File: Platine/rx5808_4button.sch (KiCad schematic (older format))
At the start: 61 parts, among them IC1 ATMEGA328-A, P1 CONN_01X02, P10 CONN_01X01, P11 CONN_01X01, P2 CONN_01X05, P3 CONN_02X03, P4 CONN_01X02, P5 BNC, P6 BNC, P7 CONN_01X02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

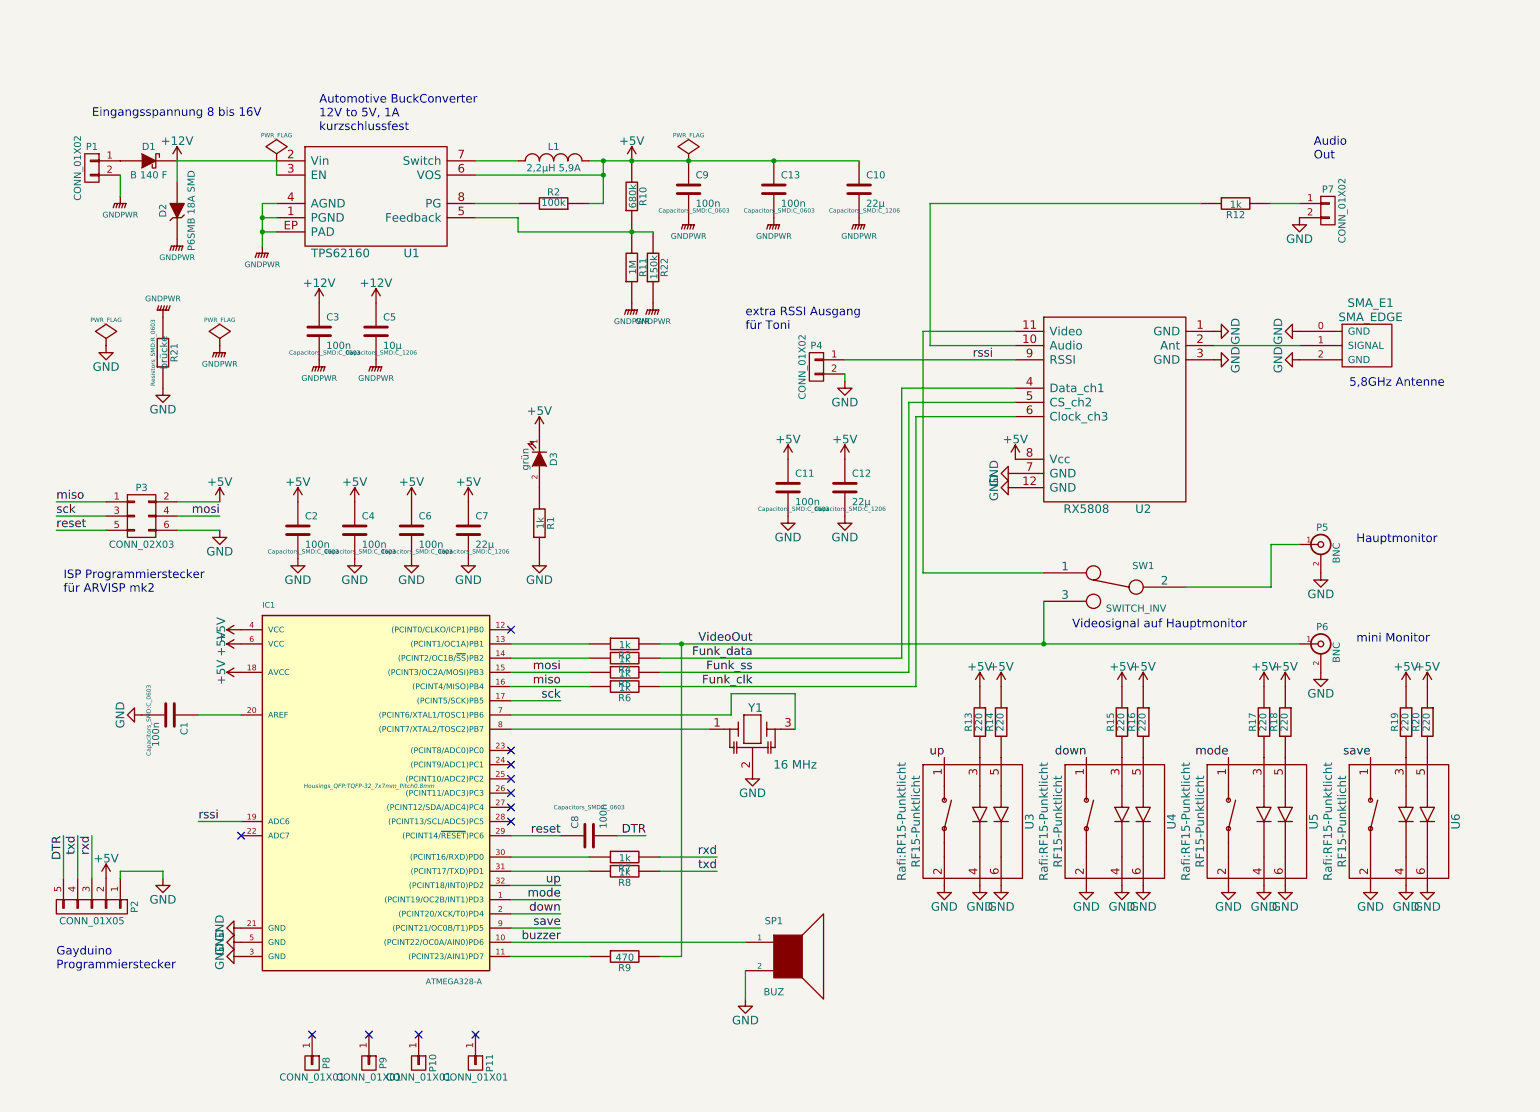
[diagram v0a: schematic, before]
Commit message: neue LIB für den micromatchstecker
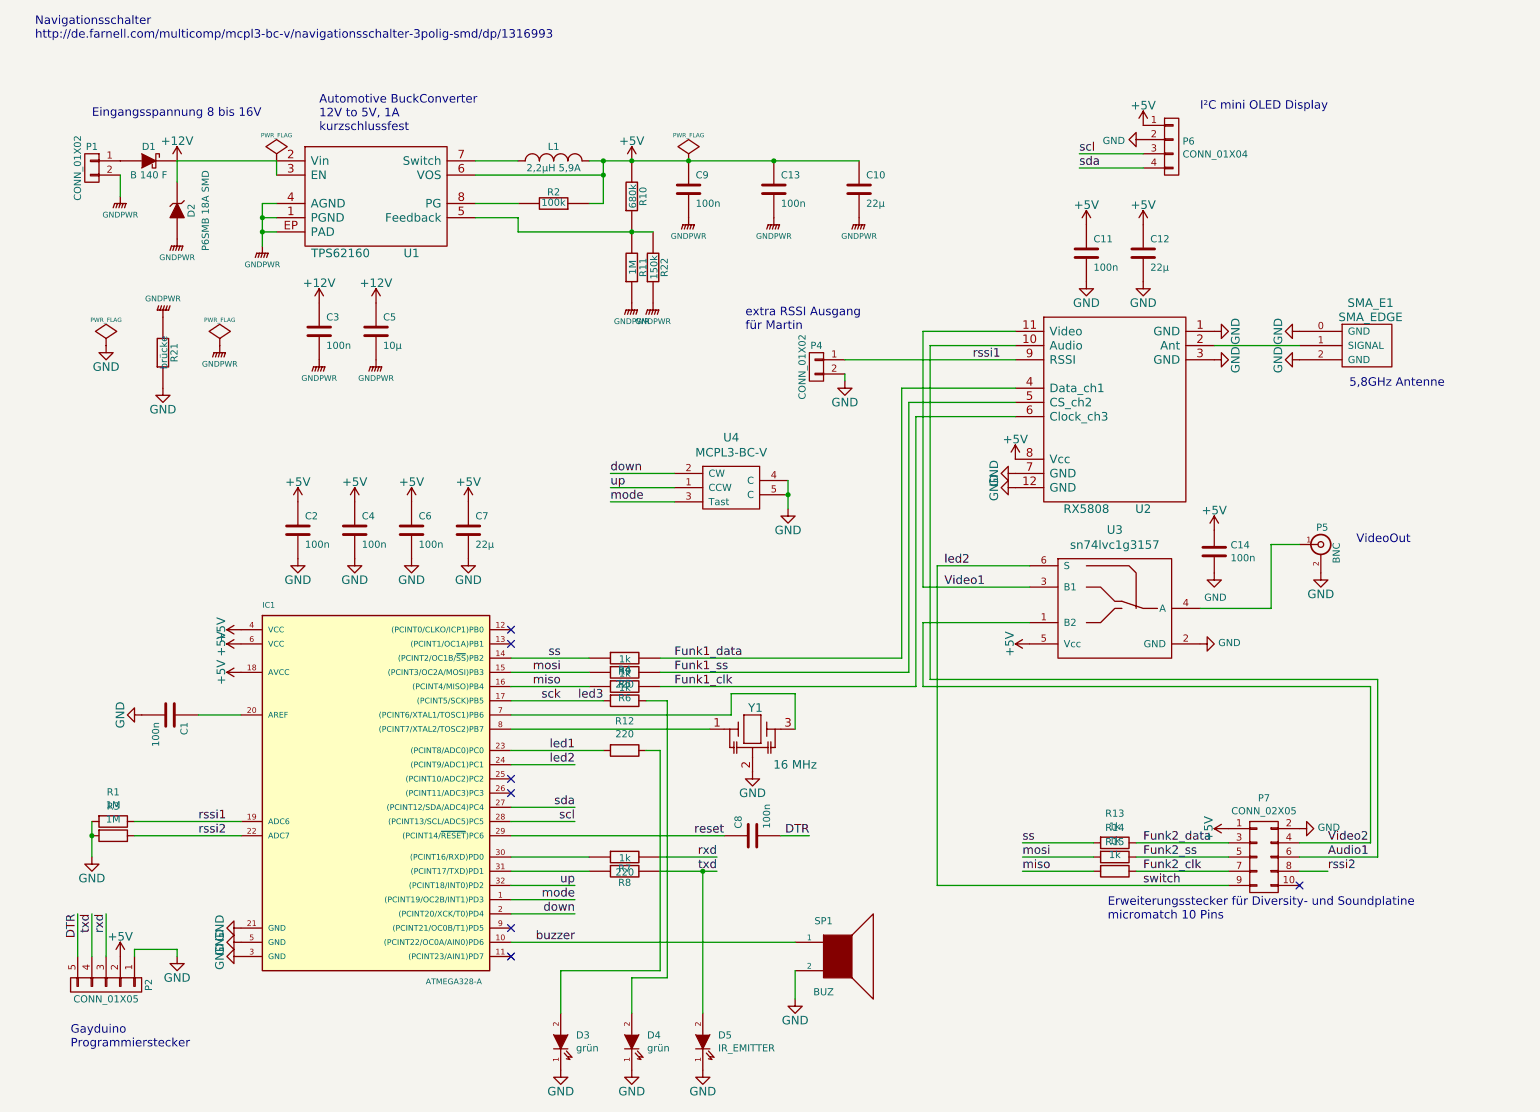
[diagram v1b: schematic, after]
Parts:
- removed P10, P11, P8, P9: CONN_01X01, Mounting_Holes:MountingHole_3-5mm, symbol CONN_01X01
- removed P3: CONN_02X03, Pin_Headers:Pin_Header_Straight_2x03, symbol CONN_02X03
- removed P6: BNC, RCA:Cinch_angled_mono, symbol BNC
- removed P7: CONN_01X02, Pin_Headers:Pin_Header_Straight_1x02, symbol CONN_01X02
- removed R1, R12, R3: 1k, Resistors_SMD:R_0603, symbol R-RESCUE-rx5808_4button
- removed R13, R14, R15, R16, R17, R18, R19, R20: 220, Resistors_SMD:R_0603, symbol R-RESCUE-rx5808_4button
- removed R9: 470, Resistors_SMD:R_0603, symbol R-RESCUE-rx5808_4button
- removed SW1: SWITCH_INV, Apem:2543xN, symbol SWITCH_INV
- removed U3, U4, U5, U6: RF15-Punktlicht, Rafi:RF15-Punktlicht, symbol RF15-Punktlicht
- added C14: 100n, Capacitors_SMD:C_0603, symbol C
- added D4: grün, LEDs:LED_0603, symbol LED
- added D5: IR_EMITTER, LEDs:LED_1206, symbol LED
- added P6: CONN_01X04, Pin_Headers:Pin_Header_Straight_1x04, symbol CONN_01X04
- added P7: CONN_02X05, spezifisch:con-amp-micromatch-MICROMATCH-10, symbol CONN_02X05
- added R1, R3: 1M, Resistors_SMD:R_0603, symbol R
- added R12, R9: 220, Resistors_SMD:R_0603, symbol R
- added R13, R14, R15: 1k, Resistors_SMD:R_0603, symbol R
- added U3: sn74lvc1g3157, TO_SOT_Packages_SMD:SC-70-6, symbol sn74lvc1g3157
- added U4: MCPL3-BC-V, symbol MCPL3-BC-V
- D1: footprint Diodes_SMD:Diode-SMA_Standard -> Diodes_SMD:SMA_Standard
- D2: footprint Diodes_SMD:Diode-SMB_Standard -> Diodes_SMD:SMB_Standard
- D3: footprint LEDs:LED-0603 -> LEDs:LED_0603
- P2: footprint Pin_Headers:Pin_Header_Straight_1x05 -> Pin_Headers:Pin_Header_Angled_1x05
- P5: footprint RCA:Cinch_angled_mono -> Pin_Headers:Pin_Header_Angled_1x02
- R8: value 1k -> 220
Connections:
- net +12V: now also D2.1 (K); no longer D2.2 (A)
- net +5V: now also C14.1, P6.1 (P1), P7.1 (P1), U3.5 (Vcc); no longer D3.1 (K)
- net GND: now also D3.1 (K), C14.2, D4.1 (K), D5.1 (K), P6.2 (P2), P7.2 (P2), R1.2, R3.2, U3.2 (GND), U4.4 (C), U4.5 (C)
- net GNDPWR: now also D2.2 (A); no longer D2.1 (K)
- net down: now also U4.2 (CW)
- net miso: now also R15.2
- net mode: now also U4.3 (Tast)
- net mosi: now also R14.2
- net txd: now also D5.2 (A)
- net up: now also U4.1 (CCW)
- net ss: now reaches IC1.14 ((PCINT2/OC1B/~SS~)PB2), R4.2
- net ss: now also R13.2
- net rssi2: now reaches IC1.22 (ADC7)
- net rssi2: now also P7.8 (P8), R3.1
- net led1: now reaches IC1.23 ((PCINT8/ADC0)PC0)
- net led1: now also R12.2
- net led2: now reaches IC1.24 ((PCINT9/ADC1)PC1)
- net led2: now also P7.9 (P9), U3.6 (S)
- net sda: now reaches IC1.27 ((PCINT12/SDA/ADC4)PC4)
- net sda: now also P6.4 (P4)
- net scl: now reaches IC1.28 ((PCINT13/SCL/ADC5)PC5)
- net scl: now also P6.3 (P3)
- net Audio1: now reaches U2.10 (Audio)
- net Audio1: now also P7.6 (P6)
- net Video1: now reaches U2.11 (Video)
- net Video1: now also U3.3 (B1)
- net at P5.1 (In): now also U3.4 (A)
- net at D3.2 (A): now also R12.1
- net Funk_clk renamed Funk1_clk
- net Funk_data renamed Funk1_data
- net Funk_ss renamed Funk1_ss
- net rssi renamed rssi1
- net rssi1: now also R1.1
- net save: no longer names the net of IC1.9 ((PCINT21/OC0B/T1)PD5)
- net sck renamed led3
- net led3: now also R9.2
- new net: D4.2 (A), R9.1
- new net Funk2_clk: P7.7 (P7), R15.1
- new net Funk2_data: P7.3 (P3), R13.1
- new net Funk2_ss: P7.5 (P5), R14.1
- new net Video2: P7.4 (P4), U3.1 (B2)
- no-connect marks 12 -> 7
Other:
- note added: "Erweiterungsstecker für Diversity- und Soundplatine\nmicromatch 10 Pins"
- note added: "I²C mini OLED Display"
- note added: "Navigationsschalter\nhttp://de.farnell.com/multicomp/mcpl3-bc-v/navigationsschalter-3polig-smd/dp/1316993"
- note added: "VideoOut"
- note added: "extra RSSI Ausgang\nfür Martin"
- note removed: "Audio\nOut"
- note removed: "Hauptmonitor"
- note removed: "ISP Programmierstecker\nfür ARVISP mk2"
- note removed: "Videosignal auf Hauptmonitor"
- note removed: "extra RSSI Ausgang\nfür Toni"
- note removed: "mini Monitor"
- moved on the sheet: C11, C12, C8, P2, SP1

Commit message: Platine fertig und exportiert.
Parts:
- removed C11: 100n, Capacitors_SMD:C_0603, symbol C-RESCUE-rx5808_4button
- removed P4: CONN_01X02, Pin_Headers:Pin_Header_Straight_1x02, symbol CONN_01X02
- L1: value 2,2µH 5,9A -> 2,2µH 1,5A; footprint TDK_Inductor:VLF4012A -> NR3015:NR3015; Digikeynummer (none) -> 587-1648-1-ND; Name VLF4012S-3R3 -> NR3015T2R2M
- SMA_E1: footprint SMA_EDGE:SMA_EDGE -> PhilippsFootprints:SMA_EDGE_small
- U4: footprint (none) -> PhilippsFootprints:MCPL3-AC-V
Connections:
- net +5V: now also SP1.1
- net GND: no longer SP1.2
- net buzzer: now also SP1.2; no longer SP1.1
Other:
- note removed: "extra RSSI Ausgang\nfür Martin"
- moved on the sheet: SP1

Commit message: Layout fertig. Überprüfung steht aus.
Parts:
- added C11: 100n, Capacitors_SMD:C_0603, symbol C
- added R16: 15k, Resistors_SMD:R_0603, symbol R
- added R17: 1k, Resistors_SMD:R_0603, symbol R
- P7: footprint spezifisch:con-amp-micromatch-MICROMATCH-10 -> PhilippsFootprints:MICROMATCH-10
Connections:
- net +12V: now also R16.2
- net GND: now also C11.2, R17.1
- net adc_12V: now reaches IC1.25 ((PCINT10/ADC2)PC2)
- net adc_12V: now also C11.1, R16.1, R17.2
- no-connect marks 7 -> 6
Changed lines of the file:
@@
 Text Notes 850  7350 0    60   ~ 0
 Gayduino\nProgrammierstecker
-NoConn ~ 3950 5450
 NoConn ~ 3950 5550
 Text Label 1750 5750 0    60   ~ 0
@@
 F 0 "P7" H 9250 6415 50  0000 C CNN
 F 1 "CONN_02X05" H 9250 6324 50  0000 C CNN
-F 2 "spezifisch:con-amp-micromatch-MICROMATCH-10" H 9250 4800 50  0001 C CNN
+F 2 "PhilippsFootprints:MICROMATCH-10" H 9250 4800 50  0001 C CNN
 F 3 "" H 9250 4800 50  0000 C CNN
 	1    9250 6000
@@
 	0    -1   -1   0
 $EndComp
+$Comp
+L R R16
+U 1 1 5709B4D9
+P 3600 2250
+F 0 "R16" V 3393 2250 50  0000 C CNN
+F 1 "15k" V 3484 2250 50  0000 C CNN
+F 2 "Resistors_SMD:R_0603" V 3530 2250 50  0001 C CNN
+F 3 "" H 3600 2250 50  0000 C CNN
+	1    3600 2250
+	-1   0    0    1
+$EndComp
+$Comp
+L +12V #PWR065
+U 1 1 5709B821
+P 3600 2100
+F 0 "#PWR065" H 3600 1950 60  0001 C CNN
+F 1 "+12V" H 3600 2240 60  0000 C CNN
+F 2 "" H 3600 2100 60  0000 C CNN
+F 3 "" H 3600 2100 60  0000 C CNN
+	1    3600 2100
+	1    0    0    -1
+$EndComp
+$Comp
+L R R17
+U 1 1 5709B8FA
+P 3600 2550
+F 0 "R17" V 3393 2550 50  0000 C CNN
+F 1 "1k" V 3484 2550 50  0000 C CNN
+F 2 "Resistors_SMD:R_0603" V 3530 2550 50  0001 C CNN
+F 3 "" H 3600 2550 50  0000 C CNN
+	1    3600 2550
+	-1   0    0    1
+$EndComp
+$Comp
+L GND #PWR066
+U 1 1 5709F4B1
+P 3600 2700
+F 0 "#PWR066" H 3600 2450 60  0001 C CNN
+F 1 "GND" H 3600 2550 60  0000 C CNN
+F 2 "" H 3600 2700 60  0000 C CNN
+F 3 "" H 3600 2700 60  0000 C CNN
+	1    3600 2700
+	1    0    0    -1
+$EndComp
+$Comp
+L GND #PWR067
+U 1 1 5709F7F4
+P 4000 2700
+F 0 "#PWR067" H 4000 2450 60  0001 C CNN
+F 1 "GND" H 4000 2550 60  0000 C CNN
+F 2 "" H 4000 2700 60  0000 C CNN
+F 3 "" H 4000 2700 60  0000 C CNN
+	1    4000 2700
+	1    0    0    -1
+$EndComp
+$Comp
+L C C11
+U 1 1 5709F89D
+P 4000 2550
+F 0 "C11" H 4115 2596 50  0000 L CNN
+F 1 "100n" H 4115 2505 50  0000 L CNN
+F 2 "Capacitors_SMD:C_0603" H 4038 2400 50  0001 C CNN
+F 3 "" H 4000 2550 50  0000 C CNN
+	1    4000 2550
+	1    0    0    -1
+$EndComp
+Wire Wire Line
+	3600 2400 4000 2400
+Text Label 4000 2400 2    60   ~ 0
+adc_12V
+Text Label 4400 5450 2    60   ~ 0
+adc_12V
+Wire Wire Line
+	4400 5450 3950 5450
 $EndSCHEMATC

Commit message: BOM für beide platinen des kompletten moduls dazugefügt
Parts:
- SMA_E1: footprint PhilippsFootprints:SMA_EDGE_small -> PhilippsFootprints:SMA_EDGE_Johnson_142-0701-801
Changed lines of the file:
@@
 F 0 "SMA_E1" H 10000 2700 60  0000 C CNN
 F 1 "SMA_EDGE" H 10000 2600 60  0000 C CNN
-F 2 "PhilippsFootprints:SMA_EDGE_small" H 9850 2400 60  0001 C CNN
+F 2 "PhilippsFootprints:SMA_EDGE_Johnson_142-0701-801" H 9850 2400 60  0001 C CNN
 F 3 "" H 9850 2400 60  0000 C CNN
 	1    9850 2400

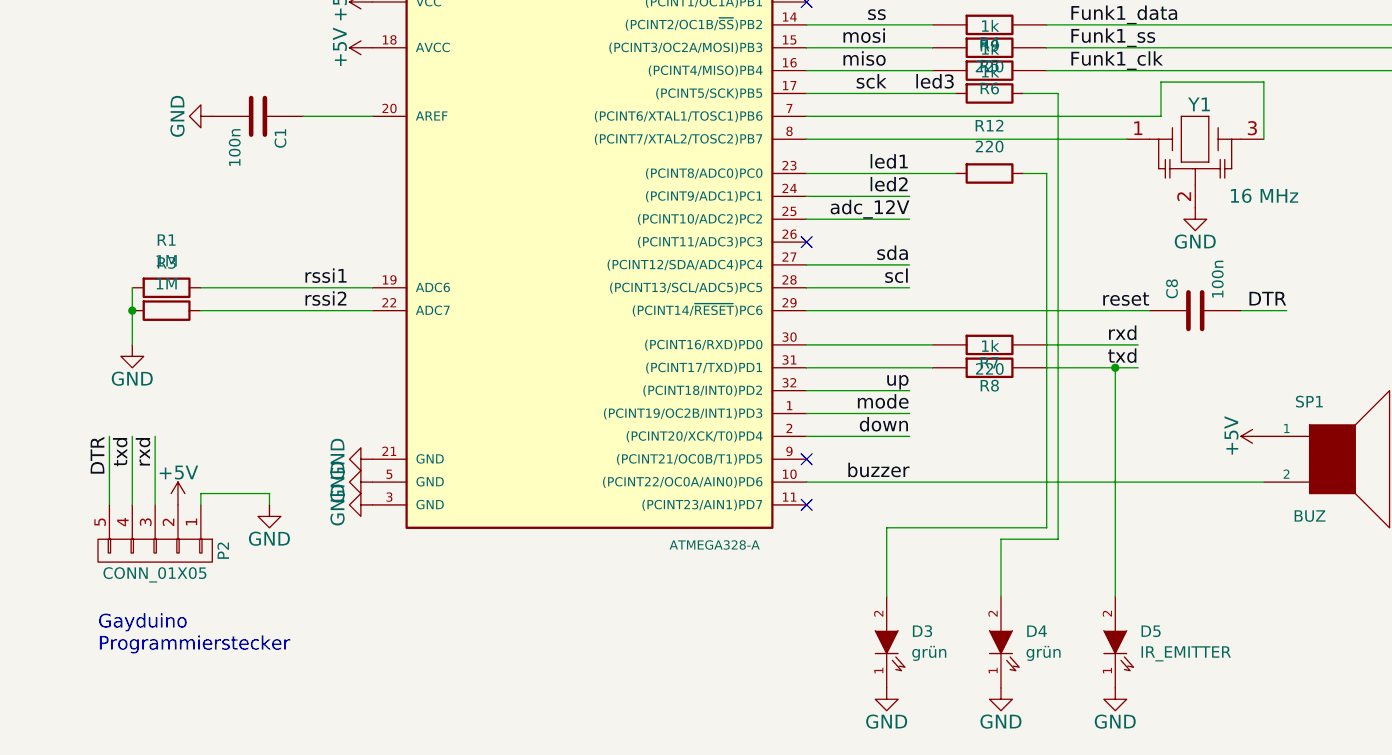
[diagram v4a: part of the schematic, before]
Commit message: schaltplan und netzliste für die beiden issues geändert.
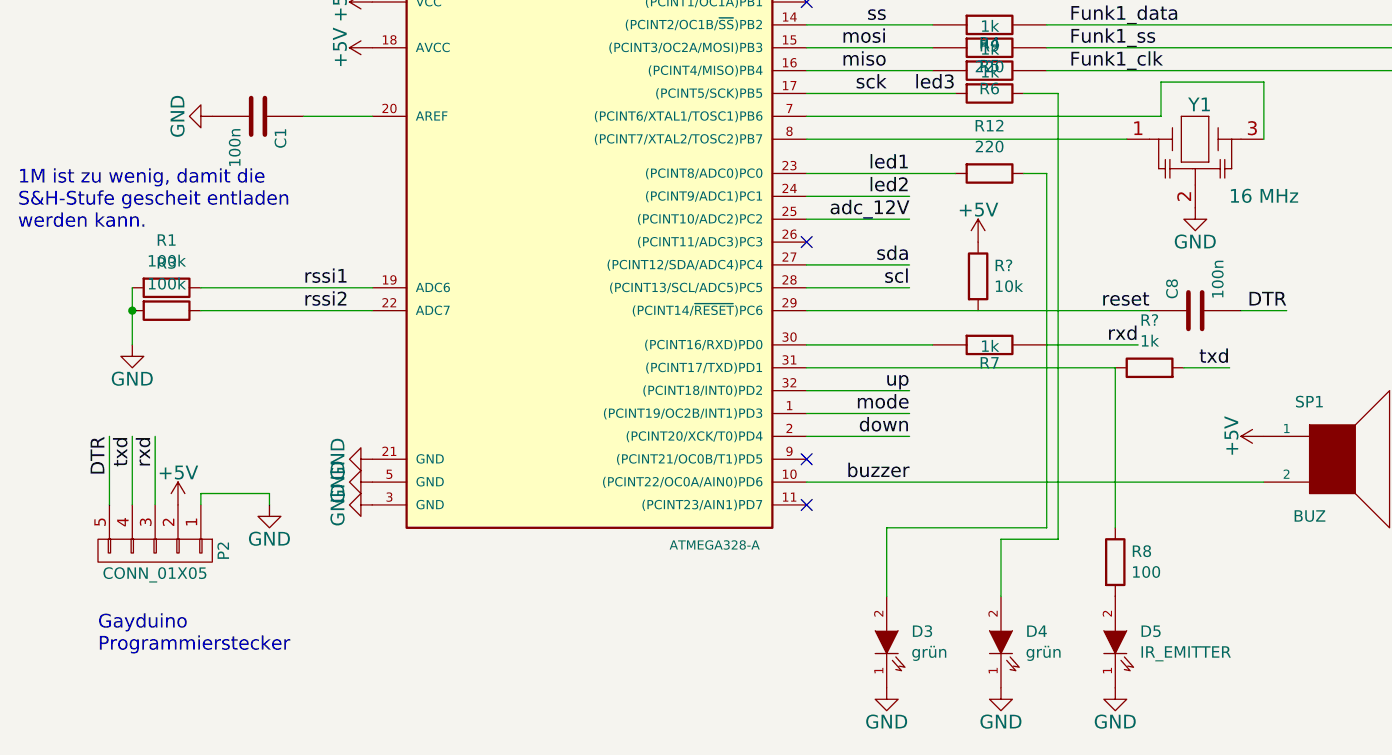
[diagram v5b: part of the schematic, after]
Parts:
- removed R8: 220, Resistors_SMD:R_0603, symbol R-RESCUE-rx5808_4button
- added R?: 100, symbol R
- added R?: 1k, symbol R
- added R?: 10k, symbol R
- R1, R3: value 1M -> 100k
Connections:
- net +5V: now also R?.1
- net txd: now also R?.2; no longer D5.2 (A)
- net at IC1.31 ((PCINT17/TXD)PD1): now also R?.1, R?.1
- new net: D5.2 (A), R?.2
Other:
- note added: "1M ist zu wenig, damit die\nS&H-Stufe gescheit entladen\nwerden kann."
